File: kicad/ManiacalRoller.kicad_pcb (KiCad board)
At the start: 2 copper layers, 0 parts

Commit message: Created HDSP-523E Footprint
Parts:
- added REF**: HDSP-523E, HDSP-523E:HDSP-523E, F.Cu at (69.8, 37.2)
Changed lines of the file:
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@@
     (tracks 0)
     (zones 0)
-    (modules 0)
+    (modules 1)
     (nets 1)
   )
@@
     (pad_to_mask_clearance 0.2)
     (aux_axis_origin 0 0)
-    (visible_elements FFFFFF7F)
+    (visible_elements 7FFFFFFF)
     (pcbplotparams
       (layerselection 0x00030_80000001)
@@
     (uvia_drill 0.1)
   )
+  (module HDSP-523E:HDSP-523E (layer F.Cu)
+    (at 69.75 37.25)
+    (descr "Afficheur 7 segments 10mm DIGIT")
+    (tags AFFICHEUR)
+    (fp_text reference REF** (at -1.1 -11.43) (layer F.SilkS)
+      (effects (font (size 1 1) (thickness 0.15)))
+    )
+    (fp_text value HDSP-523E (at -2.37 11.43) (layer F.Fab)
+      (effects (font (size 1 1) (thickness 0.15)))
+    )
+    (fp_line (start -6.25 -5.715) (end -1.805 -5.715) (layer F.SilkS) (width 0.15))
+    (fp_line (start -2.44 -0.635) (end -1.17 -5.715) (layer F.SilkS) (width 0.15))
+    (fp_line (start -8.155 -0.635) (end -6.885 -5.715) (layer F.SilkS) (width 0.15))
+    (fp_line (start -8.79 5.715) (end -4.345 5.715) (layer F.SilkS) (width 0.15))
+    (fp_line (start -8.155 0.635) (end -9.425 5.715) (layer F.SilkS) (width 0.15))
+    (fp_line (start -2.44 0.635) (end -3.71 5.715) (layer F.SilkS) (width 0.15))
+    (fp_circle (center 8.99 5.08) (end 9.625 5.08) (layer F.SilkS) (width 0.15))
+    (fp_line (start 3.91 -5.715) (end 8.355 -5.715) (layer F.SilkS) (width 0.15))
+    (fp_line (start 1.37 5.715) (end 5.815 5.715) (layer F.SilkS) (width 0.15))
+    (fp_line (start 7.72 0.635) (end 6.45 5.715) (layer F.SilkS) (width 0.15))
+    (fp_line (start 0.735 5.715) (end 2.005 0.635) (layer F.SilkS) (width 0.15))
+    (fp_line (start 7.72 -0.635) (end 8.99 -5.715) (layer F.SilkS) (width 0.15))
+    (fp_line (start 2.005 -0.635) (end 3.275 -5.715) (layer F.SilkS) (width 0.15))
+    (fp_line (start 2.64 0) (end 7.085 0) (layer F.SilkS) (width 0.15))
+    (fp_line (start 0.17 -9.525) (end 12.5 -9.525) (layer F.SilkS) (width 0.15))
+    (fp_line (start 12.5 -9.525) (end 12.5 9.525) (layer F.SilkS) (width 0.15))
+    (fp_line (start 12.5 9.525) (end 0.17 9.525) (layer F.SilkS) (width 0.15))
+    (fp_line (start -7.266 0) (end -3.202 0) (layer F.SilkS) (width 0.15))
+    (fp_circle (center -1.17 5.08) (end -0.535 5.08) (layer F.SilkS) (width 0.15))
+    (fp_line (start -11.26 -9.525) (end -12.53 -9.525) (layer F.SilkS) (width 0.15))
+    (fp_line (start -12.53 -9.525) (end -12.53 9.525) (layer F.SilkS) (width 0.15))
+    (fp_line (start -12.53 9.525) (end -11.26 9.525) (layer F.SilkS) (width 0.15))
+    (fp_line (start -1.1 9.525) (end 0.17 9.525) (layer F.SilkS) (width 0.15))
+    (fp_line (start 0.17 -9.525) (end -1.1 -9.525) (layer F.SilkS) (width 0.15))
+    (fp_line (start -11.26 9.525) (end -1.1 9.525) (layer F.SilkS) (width 0.15))
+    (fp_line (start -1.1 -9.525) (end -11.26 -9.525) (layer F.SilkS) (width 0.15))
+    (fp_line (start -7.393 0) (end -3.075 0) (layer F.SilkS) (width 0.15))
+    (pad 1 thru_hole rect (at -9.99 7.62) (size 2.032 2.032) (drill 0.9144) (layers *.Cu *.Mask))
+    (pad 2 thru_hole circle (at -7.45 7.62) (size 2.032 2.032) (drill 0.9144) (layers *.Cu *.Mask))
+    (pad 3 thru_hole circle (at -4.91 7.62) (size 2.032 2.032) (drill 0.9144) (layers *.Cu *.Mask))
+    (pad 4 thru_hole circle (at -2.37 7.62) (size 2.032 2.032) (drill 0.9144) (layers *.Cu *.Mask))
+    (pad 13 thru_hole circle (at 2.73 -7.62) (size 2.032 2.032) (drill 0.9144) (layers *.Cu *.Mask))
+    (pad 14 thru_hole circle (at 0.19 -7.62) (size 2.032 2.032) (drill 0.9144) (layers *.Cu *.Mask))
+    (pad 15 thru_hole circle (at -2.35 -7.62) (size 2.032 2.032) (drill 0.9144) (layers *.Cu *.Mask))
+    (pad 16 thru_hole circle (at -4.89 -7.62) (size 2.032 2.032) (drill 0.9144) (layers *.Cu *.Mask))
+    (pad 5 thru_hole circle (at 0.17 7.62) (size 2.032 2.032) (drill 0.9144) (layers *.Cu *.Mask))
+    (pad 6 thru_hole circle (at 2.71 7.62) (size 2.032 2.032) (drill 0.9144) (layers *.Cu *.Mask))
+    (pad 7 thru_hole circle (at 5.25 7.62) (size 2.032 2.032) (drill 0.9144) (layers *.Cu *.Mask))
+    (pad 8 thru_hole circle (at 7.79 7.62) (size 2.032 2.032) (drill 0.9144) (layers *.Cu *.Mask))
+    (pad 12 thru_hole circle (at 5.27 -7.62) (size 2.032 2.032) (drill 0.9144) (layers *.Cu *.Mask))
+    (pad 11 thru_hole circle (at 7.81 -7.62) (size 2.032 2.032) (drill 0.9144) (layers *.Cu *.Mask))
+    (pad 10 thru_hole circle (at 10.35 -7.62) (size 2.032 2.032) (drill 0.9144) (layers *.Cu *.Mask))
+    (pad 9 thru_hole circle (at 10.33 7.62) (size 2.032 2.032) (drill 0.9144) (layers *.Cu *.Mask))
+    (pad 17 thru_hole circle (at -7.43 -7.62) (size 2.032 2.032) (drill 0.9144) (layers *.Cu *.Mask))
+    (pad 18 thru_hole circle (at -9.97 -7.62) (size 2.032 2.032) (drill 0.9144) (layers *.Cu *.Mask))
+  )
 )

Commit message: PCB Layout
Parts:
- removed REF**: HDSP-523E, HDSP-523E:HDSP-523E
- added BT1: Battery, BattHolder:2xAABatteryHolder_24mm5x53mm, F.Cu at (173.5, 70.5)
- added C1: 0.1uF, Capacitors_ThroughHole:C_Disc_D3.0mm_W1.6mm_P2.50mm, F.Cu at (118.0, 43.0)
- added C2: 0.1uF, Capacitors_ThroughHole:C_Disc_D3.0mm_W1.6mm_P2.50mm, F.Cu at (133.0, 69.5)
- added CON1: AVR-ISP-6, mod:ICSP_Simple, F.Cu at (114.0, 61.5)
- added G***: LOGO, mod:logo_MLlabs_small, F.Cu at (173.0, 34.0)
- added IC1: ATMEGA328P-P, mod:DIP28, F.Cu at (120.5, 27.5)
- added Q1: Q_NPN_EBC, TO_SOT_Packages_THT:TO-92_Inline_Narrow_Oval, F.Cu at (141.0, 34.5)
- added Q2: Q_NPN_EBC, TO_SOT_Packages_THT:TO-92_Inline_Narrow_Oval, F.Cu at (147.0, 34.5)
- added R1: 100, Resistors_ThroughHole:R_Axial_DIN0204_L3.6mm_D1.6mm_P5.08mm_Horizontal, F.Cu at (146.5, 38.5)
- added R10: 100k, Resistors_ThroughHole:R_Axial_DIN0204_L3.6mm_D1.6mm_P5.08mm_Horizontal, F.Cu at (117.0, 72.0)
- added R11: 100k, Resistors_ThroughHole:R_Axial_DIN0204_L3.6mm_D1.6mm_P5.08mm_Horizontal, F.Cu at (117.0, 80.0)
- added R12: 100k, Resistors_ThroughHole:R_Axial_DIN0204_L3.6mm_D1.6mm_P5.08mm_Horizontal, F.Cu at (117.0, 88.0)
- added R13: 100k, Resistors_ThroughHole:R_Axial_DIN0204_L3.6mm_D1.6mm_P5.08mm_Horizontal, F.Cu at (117.0, 96.0)
- added R14: 100k, Resistors_ThroughHole:R_Axial_DIN0204_L3.6mm_D1.6mm_P5.08mm_Horizontal, F.Cu at (151.5, 96.0)
- added R15: 100k, Resistors_ThroughHole:R_Axial_DIN0204_L3.6mm_D1.6mm_P5.08mm_Horizontal, F.Cu at (151.5, 88.0)
- added R16: 100k, Resistors_ThroughHole:R_Axial_DIN0204_L3.6mm_D1.6mm_P5.08mm_Horizontal, F.Cu at (151.5, 80.0)
- added R17: 100k, Resistors_ThroughHole:R_Axial_DIN0204_L3.6mm_D1.6mm_P5.08mm_Horizontal, F.Cu at (151.5, 72.0)
- added R18: 1.2k, Resistors_ThroughHole:R_Axial_DIN0204_L3.6mm_D1.6mm_P5.08mm_Horizontal, F.Cu at (138.0, 35.5)
- added R19: 1.2k, Resistors_ThroughHole:R_Axial_DIN0204_L3.6mm_D1.6mm_P5.08mm_Horizontal, F.Cu at (152.5, 35.5)
- added R2: 100, Resistors_ThroughHole:R_Axial_DIN0204_L3.6mm_D1.6mm_P5.08mm_Horizontal, F.Cu at (154.0, 38.5)
- added R3: 100, Resistors_ThroughHole:R_Axial_DIN0204_L3.6mm_D1.6mm_P5.08mm_Horizontal, F.Cu at (146.0, 61.5)
- added R4: 100, Resistors_ThroughHole:R_Axial_DIN0204_L3.6mm_D1.6mm_P5.08mm_Horizontal, F.Cu at (138.5, 61.5)
- added R5: 100, Resistors_ThroughHole:R_Axial_DIN0204_L3.6mm_D1.6mm_P5.08mm_Horizontal, F.Cu at (136.0, 61.5)
- added R6: 100, Resistors_ThroughHole:R_Axial_DIN0204_L3.6mm_D1.6mm_P5.08mm_Horizontal, F.Cu at (136.5, 38.5)
- added R7: 100, Resistors_ThroughHole:R_Axial_DIN0204_L3.6mm_D1.6mm_P5.08mm_Horizontal, F.Cu at (144.0, 38.5)
- added R8: 100, Resistors_ThroughHole:R_Axial_DIN0204_L3.6mm_D1.6mm_P5.08mm_Horizontal, F.Cu at (153.5, 61.5)
- added R9: 100, Resistors_ThroughHole:R_Axial_DIN0204_L3.6mm_D1.6mm_P5.08mm_Horizontal, F.Cu at (131.5, 94.0)
- added SEG1: HDSP-523E, HDSP-523E:HDSP-523E, F.Cu at (146.0, 50.0)
- added SW1: BTN_coin, Buttons_Switches_ThroughHole:SW_PUSH_6mm, F.Cu at (126.5, 71.5)
- added SW2: BTN_d4, Buttons_Switches_ThroughHole:SW_PUSH_6mm, F.Cu at (126.5, 79.5)
- added SW3: BTN_d6, Buttons_Switches_ThroughHole:SW_PUSH_6mm, F.Cu at (126.5, 87.5)
- added SW4: BTN_d8, Buttons_Switches_ThroughHole:SW_PUSH_6mm, F.Cu at (126.5, 95.5)
- added SW5: BTN_d10, Buttons_Switches_ThroughHole:SW_PUSH_6mm, F.Cu at (148.5, 95.5)
- added SW6: BTN_d12, Buttons_Switches_ThroughHole:SW_PUSH_6mm, F.Cu at (148.5, 87.5)
- added SW7: BTN_d20, Buttons_Switches_ThroughHole:SW_PUSH_6mm, F.Cu at (148.5, 79.5)
- added SW8: BTN_d100, Buttons_Switches_ThroughHole:SW_PUSH_6mm, F.Cu at (148.5, 71.5)
- added U1: 74LS148, Housings_DIP:DIP-16_W7.62mm_Socket_LongPads, F.Cu at (138.0, 90.5)
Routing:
- net Net-(IC1-Pad14): track 0.00 -> 59.1 mm
- net Net-(IC1-Pad15): track 0.00 -> 52.2 mm, vias 0 -> 2
- net Net-(IC1-Pad10): track 0.00 -> 47.1 mm
- net MOSI: track 0.00 -> 46.7 mm
- net RST: track 0.00 -> 33.9 mm
- net Net-(IC1-Pad16): track 0.00 -> 33.7 mm
- net SCK: track 0.00 -> 31.6 mm, vias 0 -> 1
- net g: track 0.00 -> 27.5 mm
- net ONES: track 0.00 -> 27.4 mm
- net d: track 0.00 -> 25.2 mm
- net MISO: track 0.00 -> 24.9 mm, vias 0 -> 1
- net Net-(IC1-Pad9): track 0.00 -> 23.2 mm
- net f: track 0.00 -> 21.9 mm
- net dp: track 0.00 -> 21.4 mm, vias 0 -> 1
- net b: track 0.00 -> 19.8 mm
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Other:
- board text added: "10"
- board text added: "100"
- board text added: "12"
- board text added: "20"
- board text added: "4"
- board text added: "6"
- board text added: "8"
- board text added: "Maniacal Labs Maniacal Roller"
- board text added: "coin"

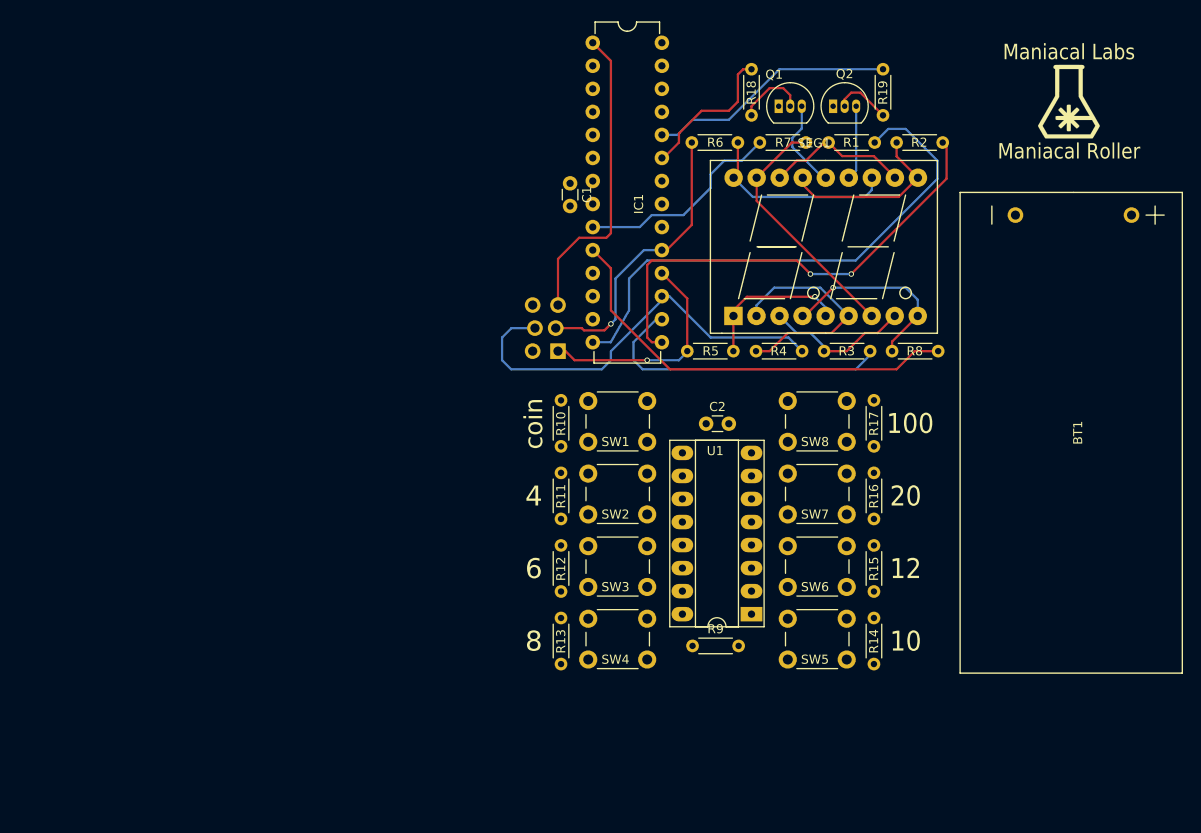
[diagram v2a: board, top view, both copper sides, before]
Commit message: Redid layout, laid tracks
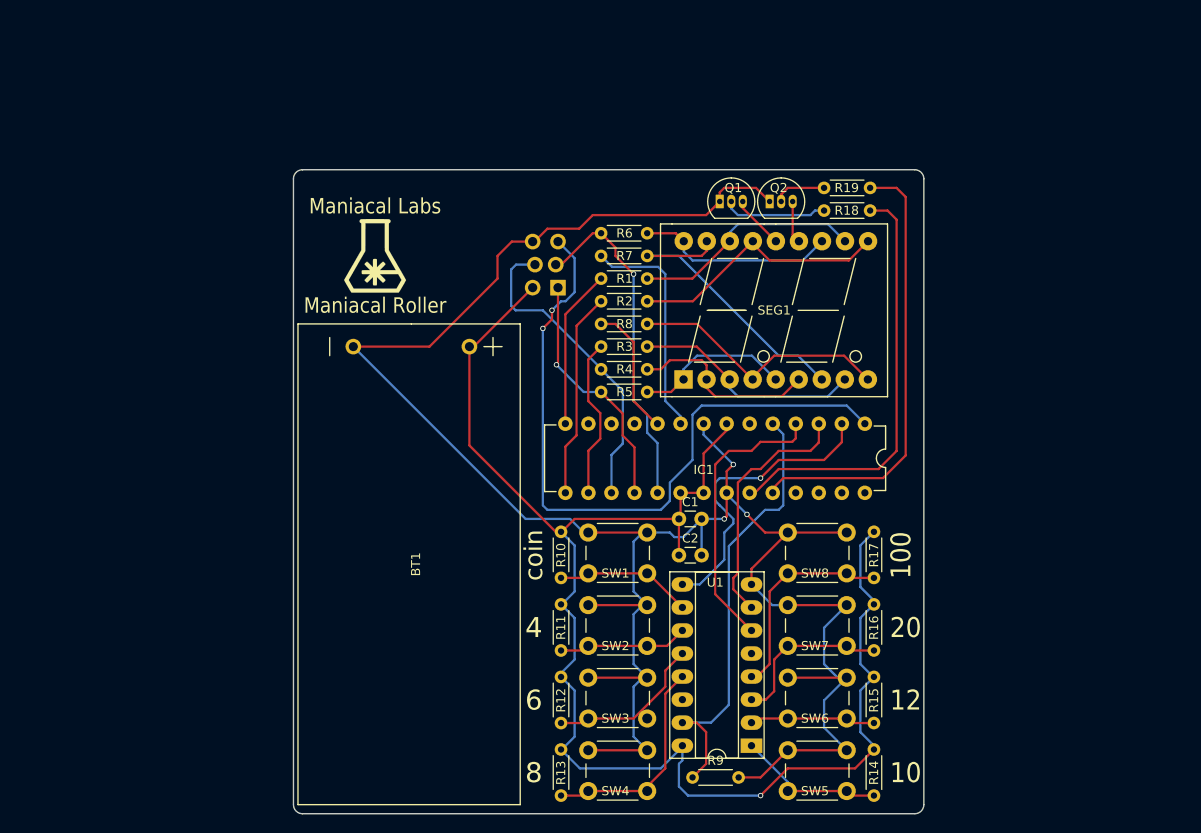
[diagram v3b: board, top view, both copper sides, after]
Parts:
- moved G*** 78.4 mm to (96.5, 51.0)
- moved BT1 74.4 mm to (100.5, 85.0)
- moved IC1 51.6 mm to (150.5, 69.5), turned to 270 degrees
- moved C1 38.9 mm to (130.0, 80.0), turned to 0 degrees
- moved R2 32.6 mm to (126.5, 56.0), turned to 180 degrees
- moved R8 27.2 mm to (126.5, 58.5), turned to 180 degrees
- moved R1 25.0 mm to (126.5, 53.5), turned to 180 degrees
- moved R7 21.5 mm to (126.5, 51.0)
- moved R3 19.5 mm to (126.5, 61.0), turned to 180 degrees
- moved C2 14.8 mm to (130.0, 84.0)
- moved R10 14.5 mm to (117.0, 86.5)
- moved R11 14.5 mm to (117.0, 94.5)
- moved R12 14.5 mm to (117.0, 102.5)
- moved R13 14.5 mm to (117.0, 110.5)
- moved R14 14.5 mm to (151.5, 110.5)
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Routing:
- net GND: track 0.00 -> 245.0 mm, vias 0 -> 3
- net VBATT: track 0.00 -> 166.0 mm, vias 0 -> 1
- net Net-(IC1-Pad5): track 0.00 -> 49.4 mm
- net RST: track 33.9 -> 77.0 mm, vias 0 -> 2
- net Net-(IC1-Pad14): track 59.1 -> 17.6 mm
- net Net-(IC1-Pad2): track 0.00 -> 33.3 mm, vias 0 -> 1
- net Net-(IC1-Pad10): track 47.1 -> 14.6 mm
- net Net-(IC1-Pad4): track 0.00 -> 31.6 mm
- net TENS: track 16.3 -> 46.9 mm
- net Net-(IC1-Pad15): track 52.2 -> 22.8 mm, vias 2 -> 0
- net Net-(IC1-Pad3): track 0.00 -> 27.6 mm
- net Net-(R13-Pad1): track 0.00 -> 23.6 mm
- net Net-(R17-Pad1): track 0.00 -> 23.1 mm
- net ONES: track 27.4 -> 49.5 mm
- net Net-(R16-Pad1): track 0.00 -> 18.2 mm
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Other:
- board outline added: 69.5 x 71 mm

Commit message: changed coin to flip, adjusted dice labels
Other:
- board text added: "flip"
- board text removed: "coin"
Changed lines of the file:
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@@
     (links 103)
     (no_connects 3)
-    (area 109.925 24.824999 185.775001 97.275001)
+    (area 87.424999 35.300001 168.85 112.575001)
     (thickness 1.6)
     (drawings 19)
@@
   )
   (gr_text 20 (at 155 92) (layer F.SilkS)
-    (effects (font (size 2.2 2) (thickness 0.3)))
+    (effects (font (size 2.2 1.9) (thickness 0.3)))
   )
   (gr_text 12 (at 155 100) (layer F.SilkS)
-    (effects (font (size 2.2 2) (thickness 0.3)))
+    (effects (font (size 2.2 1.9) (thickness 0.3)))
   )
   (gr_text 10 (at 155 108) (layer F.SilkS)
-    (effects (font (size 2.2 2) (thickness 0.3)))
+    (effects (font (size 2.2 1.9) (thickness 0.3)))
   )
   (gr_text 8 (at 114 108) (layer F.SilkS)
@@
     (effects (font (size 2.2 2.2) (thickness 0.3)))
   )
-  (gr_text coin (at 114 84 90) (layer F.SilkS)
-    (effects (font (size 2 2) (thickness 0.3)))
+  (gr_text flip (at 114 84 90) (layer F.SilkS)
+    (effects (font (size 1.9 2) (thickness 0.3)))
   )
   (segment (start 132.72 77.12) (end 132.72 72.78) (width 0.25) (layer F.Cu) (net 1))
@@
   (segment (start 130 107) (end 130 109.5) (width 0.25) (layer B.Cu) (net 1))
   (segment (start 130.38 106.62) (end 130 107) (width 0.25) (layer B.Cu) (net 1))
-  (segment (start 120 81.5) (end 119.5 81.5) (width 0.25) (layer B.Cu) (net 2) (status C00000))
-  (segment (start 119.5 81.5) (end 118 80) (width 0.25) (layer B.Cu) (net 2) (status 400000))
-  (segment (start 113.1 80) (end 94.1 61) (width 0.25) (layer B.Cu) (net 2) (status 800000))
+  (segment (start 120 81.5) (end 119.5 81.5) (width 0.25) (layer B.Cu) (net 2))
+  (segment (start 119.5 81.5) (end 118 80) (width 0.25) (layer B.Cu) (net 2))
+  (segment (start 113.1 80) (end 94.1 61) (width 0.25) (layer B.Cu) (net 2))
   (segment (start 118 80) (end 113.1 80) (width 0.25) (layer B.Cu) (net 2))
-  (segment (start 132.5 80) (end 135 80) (width 0.25) (layer B.Cu) (net 2) (status 400000))
-  (segment (start 135.26 79.74) (end 135.26 77.12) (width 0.25) (layer F.Cu) (net 2) (status 800000))
+  (segment (start 132.5 80) (end 135 80) (width 0.25) (layer B.Cu) (net 2))
+  (segment (start 135.26 79.74) (end 135.26 77.12) (width 0.25) (layer F.Cu) (net 2))
   (segment (start 135 80) (end 135.26 79.74) (width 0.25) (layer F.Cu) (net 2))
   (via (at 135 80) (size 0.6) (drill 0.4) (layers F.Cu B.Cu) (net 2))
@@
   (segment (start 132.5 67.5) (end 131.5 68.5) (width 0.25) (layer B.Cu) (net 6))
   (segment (start 148.5 67.5) (end 132.5 67.5) (width 0.25) (layer B.Cu) (net 6))
-  (segment (start 130.38 87.22) (end 132.28 87.22) (width 0.25) (layer B.Cu) (net 7) (status 400000))
+  (segment (start 130.38 87.22) (end 132.28 87.22) (width 0.25) (layer B.Cu) (net 7))
   (segment (start 139 75.5) (end 141 73.5) (width 0.25) (layer F.Cu) (net 7))
   (segment (start 141 73.5) (end 146 73.5) (width 0.25) (layer F.Cu) (net 7))
